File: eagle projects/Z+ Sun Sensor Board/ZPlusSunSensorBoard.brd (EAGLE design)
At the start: 78 x 78 mm, 54 parts, among them J1 Power In, J2 Power Out, U1 TSV991AILT, U2 ADS7841E_2K5, U4 LM20BIM7X_NOPB, U5 TSV991AILT, U8 TSV991AILT

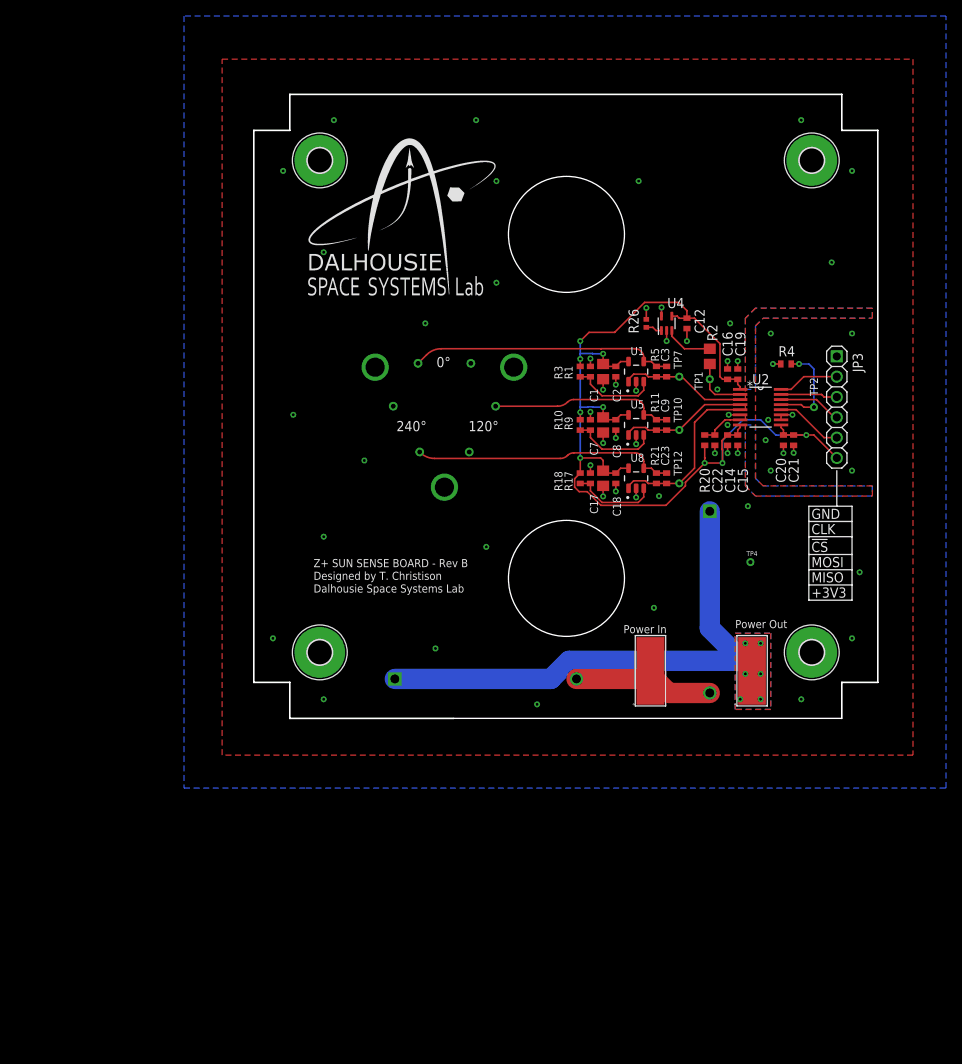
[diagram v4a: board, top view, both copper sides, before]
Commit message: Brandon changed the location of cutting resistor to top left
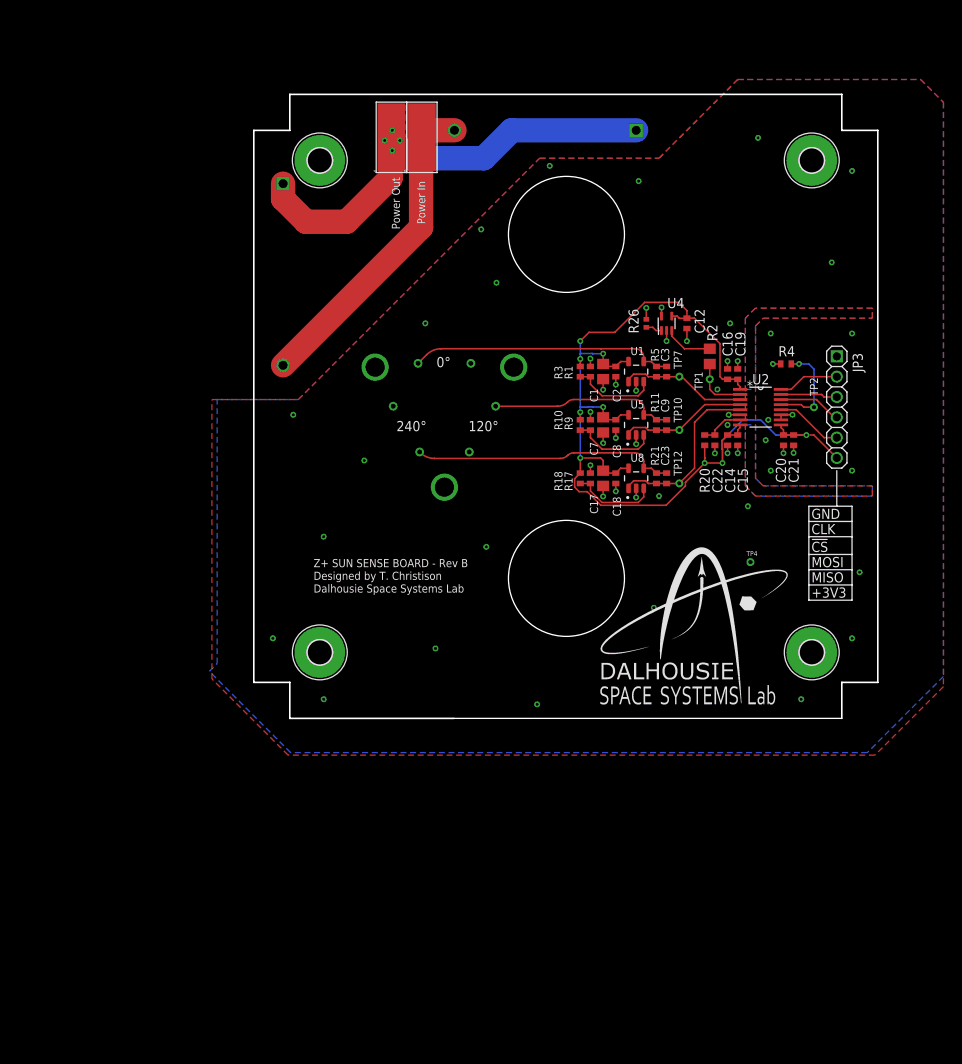
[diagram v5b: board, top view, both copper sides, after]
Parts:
- moved J2 80.5 mm to (25.4, 74.9)
- moved J1 72.5 mm to (29.2, 74.9)
- moved R7 63.5 mm to (10.2, 73.3), turned to 270 degrees
- moved R6 48.5 mm to (54.3, 80.0), turned to 0 degrees
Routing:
- net N$5: track 18.2 -> 39.9 mm
- net N$6: track 68.2 -> 56.3 mm, vias 6 -> 4
- net GND: vias 59 -> 56
- removed copper zone on layer 1, net N$6

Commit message: done z plus
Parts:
- moved J1 0.32 mm to (29.5, 74.9)
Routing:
- net N$6: track 56.3 -> 62.1 mm
- net GND: vias 56 -> 139
- removed copper zone on layer 16, net N$6

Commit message: dumb dumb fix dumb mistake
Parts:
- moved J2 8.24 mm to (21.6, 82.2), turned to 270 degrees
- moved J1 7.96 mm to (26.4, 82.2), turned to 270 degrees
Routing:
- net N$6: track 62.1 -> 61.1 mm
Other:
- board text removed: "Power In"
- board text removed: "Power Out"

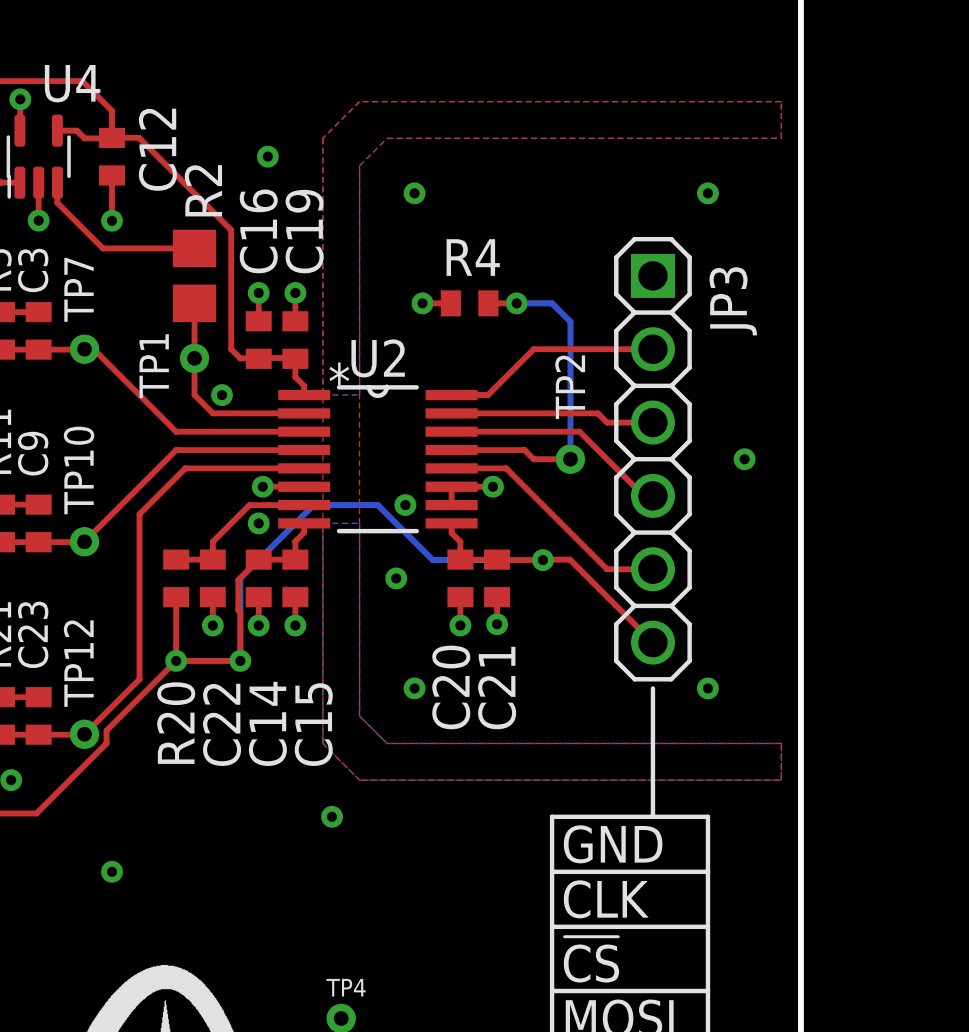
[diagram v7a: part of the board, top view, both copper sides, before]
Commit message: Solder Cups on Z+ Board
Replace previous connector on Z+ Sun Sensor Board with solder cups. Rearranged wires to fit the new component.
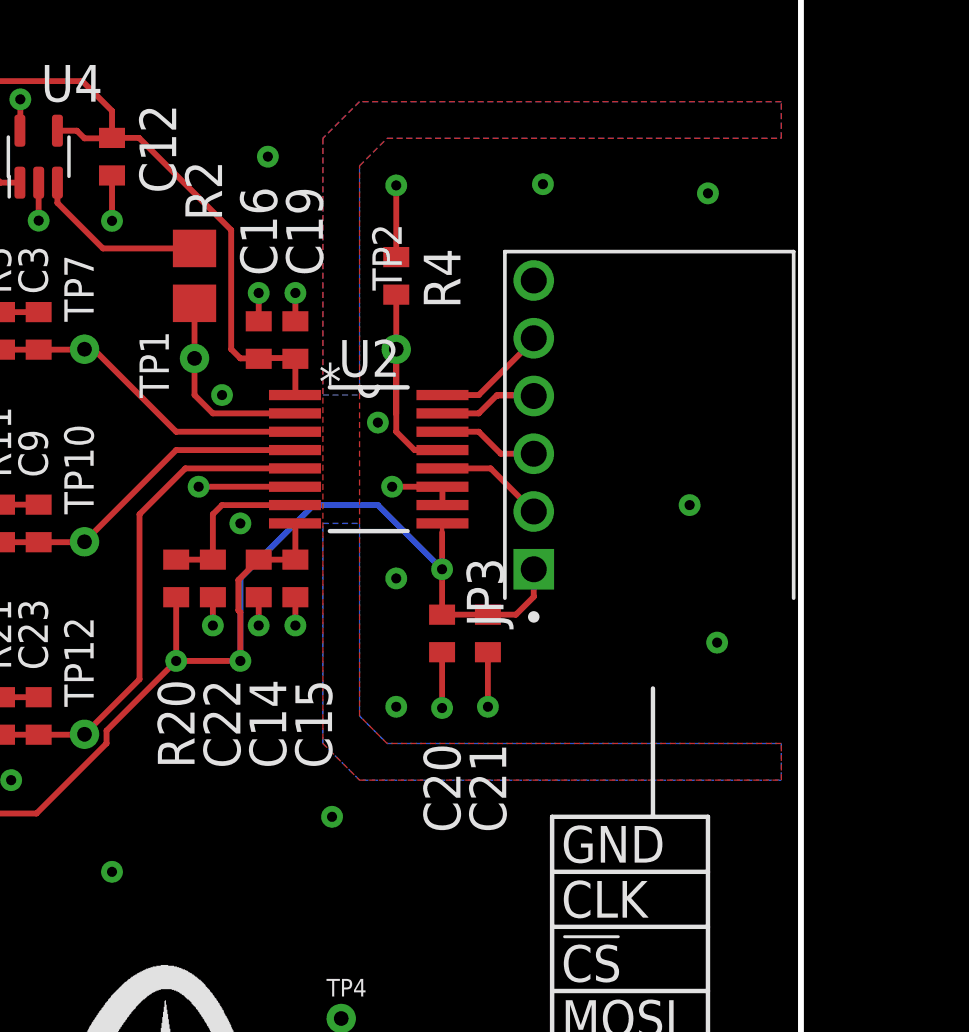
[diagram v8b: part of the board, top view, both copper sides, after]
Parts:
- JP3: value (none) -> 830-10-006-20-005000; device my_library:1X06 -> 830-10-006-20-005000:830-10-006-20-005000
- moved TP2 7.13 mm to (70.5, 49.2)
- moved JP3 5.62 mm to (75.2, 41.6), turned to 90 degrees
- moved R4 2.71 mm to (70.5, 51.8), turned to 270 degrees
- moved C20 2.01 mm to (72.1, 39.4)
- moved C21 1.93 mm to (73.7, 39.4)
- moved U2 0.32 mm to (69.5, 45.4)
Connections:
- net !CS!_SUN_Z+: now also JP3.4; no longer JP3.3
- net +3V3: now also JP3.1; no longer JP3.6
- net GND: now also JP3.6; no longer JP3.1
- net UCB0_SPI_CLK: now also JP3.5; no longer JP3.2
- net UCB0_SPI_MISO: now also JP3.2; no longer JP3.5
- net UCB0_SPI_MOSI: now also JP3.3; no longer JP3.4
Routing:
- net GND: track 29.9 -> 35.9 mm
- net +3V3: track 130.8 -> 125.4 mm
- net UCB0_SPI_MISO: track 8.42 -> 3.78 mm
- net UCB0_SPI_MOSI: track 7.89 -> 3.48 mm
- net UCB0_SPI_CLK: track 7.63 -> 4.01 mm
- net N$2: track 12.1 -> 8.87 mm, vias 1 -> 0
- net !CS!_SUN_Z+: track 7.10 -> 5.93 mm
